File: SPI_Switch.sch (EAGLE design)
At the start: 43 parts, among them Q1 MOSFET-NCHANNELBSS123LT1G, Q2 MOSFET-NCHANNELBSS123LT1G, Q3 MOSFET-NCHANNELBSS123LT1G, Q4 MOSFET-NCHANNELBSS123LT1G, Q5 MOSFET-NCHANNELBSS123LT1G, Q6 MOSFET-NCHANNELBSS123LT1G, Q7 MOSFET-NCHANNELBSS123LT1G

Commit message: adding daniel's changes
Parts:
- removed Q1, Q2, Q3, Q4, Q5, Q6, Q7: MOSFET-NCHANNELBSS123LT1G, SparkFun-DiscreteSemi:MOSFET-NCHANNELBSS123LT1G
- R5: value DNP -> 1k
- renumbered U$1 to J3, U$2 to J1, U$3 to J5, U$4 to U2, U$5 to U1, U$6 to J2, U$7 to J4
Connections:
- removed net N$10: LED5.C, Q5.D
- removed net N$12: LED6.C, Q6.D
- removed net N$14: LED7.C, Q7.D
- removed net N$2: LED1.C, Q1.D
- removed net N$4: LED2.C, Q2.D
- removed net N$6: LED3.C, Q3.D
- removed net N$8: LED4.C, Q4.D
- net +24V: now also R5.1
- net CH1: now also LED1.C; no longer J1.4_PATH1, Q1.G
- net CH2: now also LED2.C; no longer J1.6_PATH2, Q2.G
- net CH3: now also LED3.C; no longer J1.8_PATH3, Q3.G
- net CH4: now also LED4.C; no longer J1.10_PATH4, Q4.G
- net CH5: now also LED5.C; no longer J1.12_PATH5, Q5.G
- net CH6: now also LED6.C; no longer J1.14_PATH6, Q6.G
- net CH7: now also LED7.C; no longer Q7.G
- net CH8: now also R5.2; no longer R5.1
- net GND: now also U1.2_IN; no longer Q1.S, Q2.S, Q3.S, Q4.S, Q5.S, Q6.S, Q7.S, R5.2
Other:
- moved on the sheet: LED1, LED2, LED3, LED4, LED5, LED6, LED7, R10, R11, R12, R5, R6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

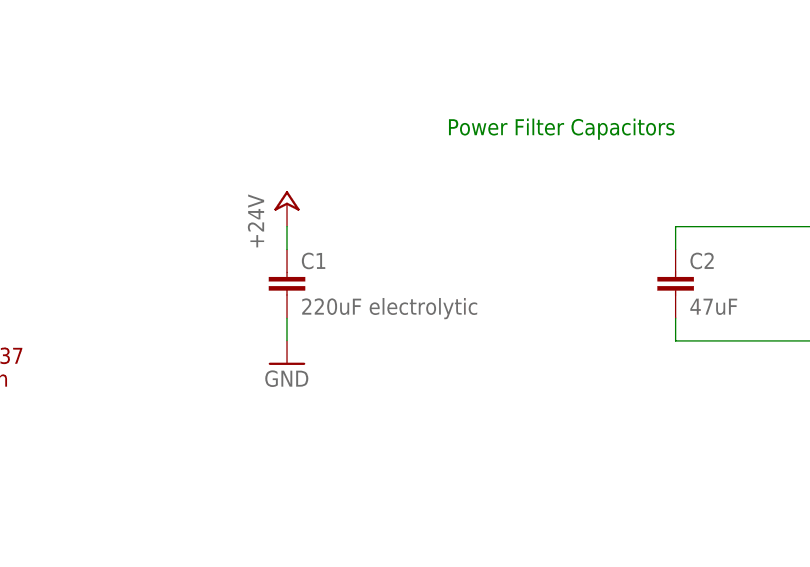
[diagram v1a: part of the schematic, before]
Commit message: Adding part numbers
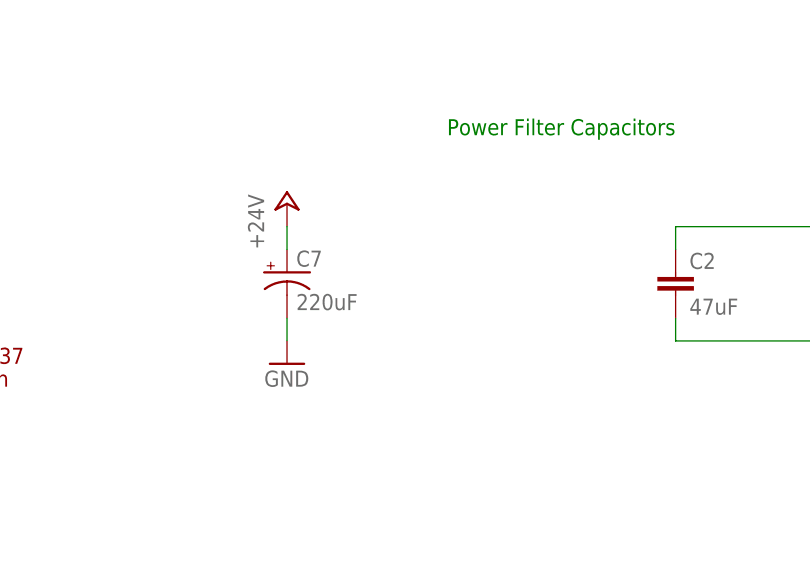
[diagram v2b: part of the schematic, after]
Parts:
- removed C1: 220uF electrolytic, SparkFun-Passives:CAP0805
- added C7: 220uF, SparkFun-Passives:CAP_POLE
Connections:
- net +24V: now also C7.+; no longer C1.1
- net GND: now also C7.-; no longer C1.2
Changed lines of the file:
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@@
 <part name="J2" library="SPI_Switch" deviceset="1-406525-1" device=""/>
 <part name="J4" library="SPI_Switch" deviceset="0705510037" device=""/>
-<part name="C1" library="SparkFun-Passives" deviceset="CAP" device="0805" value="220uF electrolytic"/>
 <part name="C2" library="SparkFun-Passives" deviceset="CAP" device="0805" value="47uF"/>
 <part name="C3" library="SparkFun-Passives" deviceset="CAP" device="0805" value="10uF"/>
@@
 <part name="P+17" library="supply1" deviceset="+24V" device=""/>
 <part name="J1" library="SPI_Switch" deviceset="8516-4500PL" device=""/>
+<part name="C7" library="SparkFun-Passives" deviceset="CAP_POL" device="E" value="220uF"/>
 </parts>
 <sheets>
@@
 <instance part="J2" gate="G$1" x="347.98" y="142.24"/>
 <instance part="J4" gate="G$1" x="104.14" y="40.64"/>
-<instance part="C1" gate="G$1" x="147.32" y="45.72"/>
 <instance part="C2" gate="G$1" x="190.5" y="45.72"/>
 <instance part="C3" gate="G$1" x="210.82" y="45.72"/>
@@
 <instance part="P+17" gate="1" x="299.72" y="335.28"/>
 <instance part="J1" gate="G$1" x="355.6" y="266.7"/>
+<instance part="C7" gate="G$1" x="147.32" y="48.26"/>
 </instances>
 <busses>
@@
 </segment>
 <segment>
-<pinref part="C1" gate="G$1" pin="2"/>
 <pinref part="GND2" gate="1" pin="GND"/>
 <wire x1="147.32" y1="43.18" x2="147.32" y2="40.64" width="0.1524" layer="91"/>
+<pinref part="C7" gate="G$1" pin="-"/>
 </segment>
 <segment>
@@
 <segment>
 <pinref part="P+3" gate="1" pin="+24V"/>
-<pinref part="C1" gate="G$1" pin="1"/>
 <wire x1="147.32" y1="53.34" x2="147.32" y2="50.8" width="0.1524" layer="91"/>
-</segment>
-<segment>
+<pinref part="C7" gate="G$1" pin="+"/>
+</segment>
+<segment>

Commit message: finished BOM
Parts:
- added LED8, LED9: YELLOW, SparkFun-LED:LED1206
- added R13: 2k, SparkFun-Passives:RESISTOR2512
- added R14: 330, SparkFun-Passives:RESISTOR0805-RES
- LED1, LED2, LED3, LED4, LED5, LED6, LED7: device led:LED -> SparkFun-LED:LED1206
- R10, R11, R12, R5, R6, R7, R8, R9: value 1k -> 2k; device SparkFun-Passives:RESISTOR0805-RES -> SparkFun-Passives:RESISTOR2512
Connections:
- new net N$2: LED8.A, R5.1
- new net N$4: LED9.A, R14.1
- net +24V: now also R10.2, R11.2, R12.2, R13.2, R5.2, R6.2, R7.2, R8.2, R9.2; no longer R10.1, R11.1, R12.1, R5.1, R6.1, R7.1, R8.1, R9.1
- net +5V: now also R14.2
- net CH8: now also R13.1; no longer R5.2
- net GND: now also LED8.C, LED9.C
- net N$1: now also R6.1; no longer R7.2
- net N$11: now also R11.1; no longer R11.2
- net N$13: now also R12.1; no longer R12.2
- net N$3: now also R7.1; no longer R6.2
- net N$5: now also R8.1; no longer R8.2
- net N$7: now also R9.1; no longer R9.2
- net N$9: now also R10.1; no longer R10.2
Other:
- note added: "Power Indication LEDs"
- moved on the sheet: R10, R11, R12, R5, R6, R7, R8, R9

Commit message: Finished layout, must do routing now
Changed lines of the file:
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@@
 <pinref part="U1" gate="G$1" pin="21_OUT0"/>
 <wire x1="180.34" y1="297.18" x2="208.28" y2="297.18" width="0.1524" layer="91"/>
-<wire x1="208.28" y1="297.18" x2="342.9" y2="297.18" width="0.1524" layer="91"/>
 <label x="187.96" y="297.18" size="1.778" layer="95"/>
 <label x="325.12" y="297.18" size="1.778" layer="95"/>
-<wire x1="208.28" y1="309.88" x2="208.28" y2="297.18" width="0.1524" layer="91"/>
-<junction x="208.28" y="297.18"/>
+<wire x1="208.28" y1="297.18" x2="342.9" y2="297.18" width="0.1524" layer="91"/>
 <wire x1="342.9" y1="297.18" x2="342.9" y2="302.26" width="0.1524" layer="91"/>
 <wire x1="342.9" y1="302.26" x2="350.52" y2="302.26" width="0.1524" layer="91"/>
 <pinref part="J1" gate="G$1" pin="3_PATH1"/>
 <pinref part="LED1" gate="G$1" pin="C"/>
-</segment>
-</net>
-<net name="N$1" class="0">
-<segment>
-<wire x1="208.28" y1="317.5" x2="208.28" y2="320.04" width="0.1524" layer="91"/>
-<pinref part="LED1" gate="G$1" pin="A"/>
-<pinref part="R6" gate="G$1" pin="1"/>
+<wire x1="208.28" y1="309.88" x2="208.28" y2="297.18" width="0.1524" layer="91"/>
+<junction x="208.28" y="297.18"/>
 </segment>
 </net>
@@
 <label x="187.96" y="294.64" size="1.778" layer="95"/>
 <label x="325.12" y="294.64" size="1.778" layer="95"/>
+<pinref part="J1" gate="G$1" pin="5_PATH2"/>
+<pinref part="LED2" gate="G$1" pin="C"/>
 <wire x1="220.98" y1="309.88" x2="220.98" y2="294.64" width="0.1524" layer="91"/>
 <junction x="220.98" y="294.64"/>
-<pinref part="J1" gate="G$1" pin="5_PATH2"/>
-<pinref part="LED2" gate="G$1" pin="C"/>
 </segment>
 </net>
@@
 <pinref part="U1" gate="G$1" pin="3_OUT2"/>
 <wire x1="180.34" y1="292.1" x2="233.68" y2="292.1" width="0.1524" layer="91"/>
-<wire x1="233.68" y1="292.1" x2="350.52" y2="292.1" width="0.1524" layer="91"/>
 <label x="187.96" y="292.1" size="1.778" layer="95"/>
 <label x="325.12" y="292.1" size="1.778" layer="95"/>
+<pinref part="J1" gate="G$1" pin="7_PATH3"/>
+<pinref part="LED3" gate="G$1" pin="C"/>
+<wire x1="233.68" y1="292.1" x2="350.52" y2="292.1" width="0.1524" layer="91"/>
 <wire x1="233.68" y1="309.88" x2="233.68" y2="292.1" width="0.1524" layer="91"/>
 <junction x="233.68" y="292.1"/>
-<pinref part="J1" gate="G$1" pin="7_PATH3"/>
-<pinref part="LED3" gate="G$1" pin="C"/>
 </segment>
 </net>
@@
 <pinref part="U1" gate="G$1" pin="4_OUT3"/>
 <wire x1="180.34" y1="289.56" x2="246.38" y2="289.56" width="0.1524" layer="91"/>
-<wire x1="246.38" y1="289.56" x2="345.44" y2="289.56" width="0.1524" layer="91"/>
 <label x="187.96" y="289.56" size="1.778" layer="95"/>
 <label x="325.12" y="289.56" size="1.778" layer="95"/>
-<wire x1="246.38" y1="309.88" x2="246.38" y2="289.56" width="0.1524" layer="91"/>
-<junction x="246.38" y="289.56"/>
+<wire x1="246.38" y1="289.56" x2="345.44" y2="289.56" width="0.1524" layer="91"/>
 <wire x1="345.44" y1="289.56" x2="345.44" y2="287.02" width="0.1524" layer="91"/>
 <wire x1="345.44" y1="287.02" x2="350.52" y2="287.02" width="0.1524" layer="91"/>
 <pinref part="J1" gate="G$1" pin="9_PATH4"/>
 <pinref part="LED4" gate="G$1" pin="C"/>
+<wire x1="246.38" y1="309.88" x2="246.38" y2="289.56" width="0.1524" layer="91"/>
+<junction x="246.38" y="289.56"/>
 </segment>
 </net>
@@
 <pinref part="U1" gate="G$1" pin="9_OUT4"/>
 <wire x1="180.34" y1="287.02" x2="259.08" y2="287.02" width="0.1524" layer="91"/>
-<wire x1="259.08" y1="287.02" x2="342.9" y2="287.02" width="0.1524" layer="91"/>
 <label x="187.96" y="287.02" size="1.778" layer="95"/>
 <label x="325.12" y="287.02" size="1.778" layer="95"/>
-<wire x1="259.08" y1="309.88" x2="259.08" y2="287.02" width="0.1524" layer="91"/>
-<junction x="259.08" y="287.02"/>
+<wire x1="259.08" y1="287.02" x2="342.9" y2="287.02" width="0.1524" layer="91"/>
 <wire x1="342.9" y1="287.02" x2="342.9" y2="281.94" width="0.1524" layer="91"/>
 <wire x1="342.9" y1="281.94" x2="350.52" y2="281.94" width="0.1524" layer="91"/>
 <pinref part="J1" gate="G$1" pin="11_PATH5"/>
 <pinref part="LED5" gate="G$1" pin="C"/>
+<wire x1="259.08" y1="309.88" x2="259.08" y2="287.02" width="0.1524" layer="91"/>
+<junction x="259.08" y="287.02"/>
 </segment>
 </net>
@@
 <pinref part="U1" gate="G$1" pin="10_OUT5"/>
 <wire x1="180.34" y1="284.48" x2="271.78" y2="284.48" width="0.1524" layer="91"/>
-<wire x1="271.78" y1="284.48" x2="340.36" y2="284.48" width="0.1524" layer="91"/>
 <label x="187.96" y="284.48" size="1.778" layer="95"/>
 <label x="325.12" y="284.48" size="1.778" layer="95"/>
-<wire x1="271.78" y1="309.88" x2="271.78" y2="284.48" width="0.1524" layer="91"/>
-<junction x="271.78" y="284.48"/>
+<wire x1="271.78" y1="284.48" x2="340.36" y2="284.48" width="0.1524" layer="91"/>
 <wire x1="340.36" y1="284.48" x2="340.36" y2="276.86" width="0.1524" layer="91"/>
 <wire x1="340.36" y1="276.86" x2="350.52" y2="276.86" width="0.1524" layer="91"/>
 <pinref part="J1" gate="G$1" pin="13_PATH6"/>
 <pinref part="LED6" gate="G$1" pin="C"/>
+<wire x1="271.78" y1="309.88" x2="271.78" y2="284.48" width="0.1524" layer="91"/>
+<junction x="271.78" y="284.48"/>
 </segment>
 </net>
@@
 <label x="187.96" y="281.94" size="1.778" layer="95"/>
 <label x="325.12" y="281.94" size="1.778" layer="95"/>
+<pinref part="J1" gate="G$1" pin="16_OPENALL"/>
+<pinref part="LED7" gate="G$1" pin="C"/>
 <wire x1="284.48" y1="309.88" x2="284.48" y2="281.94" width="0.1524" layer="91"/>
 <junction x="284.48" y="281.94"/>
-<pinref part="J1" gate="G$1" pin="16_OPENALL"/>
-<pinref part="LED7" gate="G$1" pin="C"/>
-</segment>
-</net>
-<net name="N$3" class="0">
-<segment>
-<wire x1="220.98" y1="317.5" x2="220.98" y2="320.04" width="0.1524" layer="91"/>
-<pinref part="LED2" gate="G$1" pin="A"/>
-<pinref part="R7" gate="G$1" pin="1"/>
-</segment>
-</net>
-<net name="N$5" class="0">
-<segment>
-<wire x1="233.68" y1="317.5" x2="233.68" y2="320.04" width="0.1524" layer="91"/>
-<pinref part="LED3" gate="G$1" pin="A"/>
-<pinref part="R8" gate="G$1" pin="1"/>
-</segment>
-</net>
-<net name="N$7" class="0">
-<segment>
-<wire x1="246.38" y1="317.5" x2="246.38" y2="320.04" width="0.1524" layer="91"/>
-<pinref part="LED4" gate="G$1" pin="A"/>
-<pinref part="R9" gate="G$1" pin="1"/>
-</segment>
-</net>
-<net name="N$9" class="0">
-<segment>
-<wire x1="259.08" y1="317.5" x2="259.08" y2="320.04" width="0.1524" layer="91"/>
-<pinref part="LED5" gate="G$1" pin="A"/>
-<pinref part="R10" gate="G$1" pin="1"/>
-</segment>
-</net>
-<net name="N$11" class="0">
-<segment>
-<wire x1="271.78" y1="317.5" x2="271.78" y2="320.04" width="0.1524" layer="91"/>
-<pinref part="LED6" gate="G$1" pin="A"/>
-<pinref part="R11" gate="G$1" pin="1"/>
-</segment>
-</net>
-<net name="N$13" class="0">
-<segment>
-<wire x1="284.48" y1="317.5" x2="284.48" y2="320.04" width="0.1524" layer="91"/>
-<pinref part="LED7" gate="G$1" pin="A"/>
-<pinref part="R12" gate="G$1" pin="1"/>
 </segment>
 </net>
@@
 </segment>
 </net>
+<net name="N$1" class="0">
+<segment>
+<pinref part="LED1" gate="G$1" pin="A"/>
+<pinref part="R6" gate="G$1" pin="1"/>
+<wire x1="208.28" y1="317.5" x2="208.28" y2="320.04" width="0.1524" layer="91"/>
+</segment>
+</net>
+<net name="N$3" class="0">
+<segment>
+<pinref part="R7" gate="G$1" pin="1"/>
+<pinref part="LED2" gate="G$1" pin="A"/>
+<wire x1="220.98" y1="320.04" x2="220.98" y2="317.5" width="0.1524" layer="91"/>
+</segment>
+</net>
+<net name="N$5" class="0">
+<segment>
+<pinref part="R8" gate="G$1" pin="1"/>
+<pinref part="LED3" gate="G$1" pin="A"/>
+<wire x1="233.68" y1="320.04" x2="233.68" y2="317.5" width="0.1524" layer="91"/>
+</segment>
+</net>
+<net name="N$6" class="0">
+<segment>
+<pinref part="R9" gate="G$1" pin="1"/>
+<pinref part="LED4" gate="G$1" pin="A"/>
+<wire x1="246.38" y1="320.04" x2="246.38" y2="317.5" width="0.1524" layer="91"/>
+</segment>
+</net>
+<net name="N$7" class="0">
+<segment>
+<pinref part="R10" gate="G$1" pin="1"/>
+<pinref part="LED5" gate="G$1" pin="A"/>
+<wire x1="259.08" y1="320.04" x2="259.08" y2="317.5" width="0.1524" layer="91"/>
+</segment>
+</net>
+<net name="N$8" class="0">
+<segment>
+<pinref part="R11" gate="G$1" pin="1"/>
+<pinref part="LED6" gate="G$1" pin="A"/>
+<wire x1="271.78" y1="320.04" x2="271.78" y2="317.5" width="0.1524" layer="91"/>
+</segment>
+</net>
+<net name="N$9" class="0">
+<segment>
+<pinref part="R12" gate="G$1" pin="1"/>
+<pinref part="LED7" gate="G$1" pin="A"/>
+<wire x1="284.48" y1="320.04" x2="284.48" y2="317.5" width="0.1524" layer="91"/>
+</segment>
+</net>

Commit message: Added channel routings
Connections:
- net CE: now also U1.1_CS
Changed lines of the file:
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@@
 <pinref part="R4" gate="G$1" pin="1"/>
 <wire x1="185.42" y1="101.6" x2="233.68" y2="101.6" width="0.1524" layer="91"/>
+<pinref part="U1" gate="G$1" pin="1_CS"/>
 </segment>
 </net>

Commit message: Finished routing except ground plane
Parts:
- removed C6: 10uF, SparkFun-Passives:CAP0805
- added C1: (no value), SparkFun-Passives:CAP0402-CAP
- C5: value 10uF -> (none); device SparkFun-Passives:CAP0805 -> SparkFun-Passives:CAP0402-CAP
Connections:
- net +5V: now also C1.1; no longer C6.1
- net GND: now also C1.2; no longer C6.2
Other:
- moved on the sheet: C5
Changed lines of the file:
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@@
 <part name="P+6" library="supply1" deviceset="+5V" device=""/>
 <part name="GND7" library="supply1" deviceset="GND" device=""/>
-<part name="C5" library="SparkFun-Passives" deviceset="CAP" device="0805" value="10uF"/>
-<part name="C6" library="SparkFun-Passives" deviceset="CAP" device="0805" value="10uF"/>
 <part name="P+7" library="supply1" deviceset="+5V" device=""/>
 <part name="P+8" library="supply1" deviceset="+5V" device=""/>
@@
 <part name="R13" library="SparkFun-Passives" deviceset="RESISTOR" device="2512" value="2k"/>
 <part name="R14" library="SparkFun-Passives" deviceset="RESISTOR" device="0805-RES" value="330"/>
+<part name="C1" library="SparkFun-Passives" deviceset="CAP" device="0402-CAP"/>
+<part name="C5" library="SparkFun-Passives" deviceset="CAP" device="0402-CAP"/>
 </parts>
 <sheets>
@@
 <instance part="P+6" gate="1" x="231.14" y="182.88"/>
 <instance part="GND7" gate="1" x="340.36" y="137.16"/>
-<instance part="C5" gate="G$1" x="81.28" y="302.26"/>
-<instance part="C6" gate="G$1" x="96.52" y="302.26"/>
 <instance part="P+7" gate="1" x="81.28" y="312.42"/>
 <instance part="P+8" gate="1" x="96.52" y="312.42"/>
@@
 <instance part="R13" gate="G$1" x="299.72" y="325.12" rot="R90"/>
 <instance part="R14" gate="G$1" x="96.52" y="363.22" rot="R90"/>
+<instance part="C1" gate="G$1" x="81.28" y="302.26"/>
+<instance part="C5" gate="G$1" x="96.52" y="302.26"/>
 </instances>
 <busses>
@@
 </segment>
 <segment>
-<pinref part="C5" gate="G$1" pin="2"/>
 <wire x1="81.28" y1="299.72" x2="81.28" y2="297.18" width="0.1524" layer="91"/>
 <pinref part="GND8" gate="1" pin="GND"/>
-</segment>
-<segment>
-<pinref part="C6" gate="G$1" pin="2"/>
+<pinref part="C1" gate="G$1" pin="2"/>
+</segment>
+<segment>
 <wire x1="96.52" y1="299.72" x2="96.52" y2="297.18" width="0.1524" layer="91"/>
 <pinref part="GND9" gate="1" pin="GND"/>
+<pinref part="C5" gate="G$1" pin="2"/>
 </segment>
 <segment>
@@
 </segment>
 <segment>
-<pinref part="C5" gate="G$1" pin="1"/>
 <wire x1="81.28" y1="307.34" x2="81.28" y2="309.88" width="0.1524" layer="91"/>
 <pinref part="P+7" gate="1" pin="+5V"/>
-</segment>
-<segment>
-<pinref part="C6" gate="G$1" pin="1"/>
+<pinref part="C1" gate="G$1" pin="1"/>
+</segment>
+<segment>
 <wire x1="96.52" y1="307.34" x2="96.52" y2="309.88" width="0.1524" layer="91"/>
 <pinref part="P+8" gate="1" pin="+5V"/>
-</segment>
-<segment>
+<pinref part="C5" gate="G$1" pin="1"/>
+</segment>
+<segment>

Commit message: Replaced decoupling caps for line driver with a larger package. Added smaller resistors for LEDs. Must ensure we never pull over 20mA with this resistor package.
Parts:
- C1, C5: value (none) -> 10uF; device SparkFun-Passives:CAP0402-CAP -> SparkFun-Passives:CAP0805
- R10, R11, R12, R13, R6, R7, R8, R9: value 2k -> 1.5k; device SparkFun-Passives:RESISTOR2512 -> SparkFun-Passives:RESISTOR1206
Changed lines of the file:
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@@
 <part name="P+19" library="supply1" deviceset="+5V" device=""/>
 <part name="R5" library="SparkFun-Passives" deviceset="RESISTOR" device="2512" value="2k"/>
-<part name="R6" library="SparkFun-Passives" deviceset="RESISTOR" device="2512" value="2k"/>
-<part name="R7" library="SparkFun-Passives" deviceset="RESISTOR" device="2512" value="2k"/>
-<part name="R8" library="SparkFun-Passives" deviceset="RESISTOR" device="2512" value="2k"/>
-<part name="R9" library="SparkFun-Passives" deviceset="RESISTOR" device="2512" value="2k"/>
-<part name="R10" library="SparkFun-Passives" deviceset="RESISTOR" device="2512" value="2k"/>
-<part name="R11" library="SparkFun-Passives" deviceset="RESISTOR" device="2512" value="2k"/>
-<part name="R12" library="SparkFun-Passives" deviceset="RESISTOR" device="2512" value="2k"/>
-<part name="R13" library="SparkFun-Passives" deviceset="RESISTOR" device="2512" value="2k"/>
 <part name="R14" library="SparkFun-Passives" deviceset="RESISTOR" device="0805-RES" value="330"/>
-<part name="C1" library="SparkFun-Passives" deviceset="CAP" device="0402-CAP"/>
-<part name="C5" library="SparkFun-Passives" deviceset="CAP" device="0402-CAP"/>
+<part name="C1" library="SparkFun-Passives" deviceset="CAP" device="0805" value="10uF"/>
+<part name="C5" library="SparkFun-Passives" deviceset="CAP" device="0805" value="10uF"/>
+<part name="R6" library="SparkFun-Passives" deviceset="RESISTOR" device="1206" value="1.5k"/>
+<part name="R7" library="SparkFun-Passives" deviceset="RESISTOR" device="1206" value="1.5k"/>
+<part name="R8" library="SparkFun-Passives" deviceset="RESISTOR" device="1206" value="1.5k"/>
+<part name="R9" library="SparkFun-Passives" deviceset="RESISTOR" device="1206" value="1.5k"/>
+<part name="R10" library="SparkFun-Passives" deviceset="RESISTOR" device="1206" value="1.5k"/>
+<part name="R11" library="SparkFun-Passives" deviceset="RESISTOR" device="1206" value="1.5k"/>
+<part name="R12" library="SparkFun-Passives" deviceset="RESISTOR" device="1206" value="1.5k"/>
+<part name="R13" library="SparkFun-Passives" deviceset="RESISTOR" device="1206" value="1.5k"/>
 </parts>
 <sheets>
@@
 <instance part="P+19" gate="1" x="96.52" y="373.38"/>
 <instance part="R5" gate="G$1" x="81.28" y="363.22" rot="R90"/>
+<instance part="R14" gate="G$1" x="96.52" y="363.22" rot="R90"/>
+<instance part="C1" gate="G$1" x="81.28" y="302.26"/>
+<instance part="C5" gate="G$1" x="96.52" y="302.26"/>
 <instance part="R6" gate="G$1" x="208.28" y="325.12" rot="R90"/>
 <instance part="R7" gate="G$1" x="220.98" y="325.12" rot="R90"/>
@@
 <instance part="R12" gate="G$1" x="284.48" y="325.12" rot="R90"/>
 <instance part="R13" gate="G$1" x="299.72" y="325.12" rot="R90"/>
-<instance part="R14" gate="G$1" x="96.52" y="363.22" rot="R90"/>
-<instance part="C1" gate="G$1" x="81.28" y="302.26"/>
-<instance part="C5" gate="G$1" x="96.52" y="302.26"/>
 </instances>
 <busses>
@@
 <segment>
 <pinref part="LED1" gate="G$1" pin="A"/>
+<wire x1="208.28" y1="317.5" x2="208.28" y2="320.04" width="0.1524" layer="91"/>
 <pinref part="R6" gate="G$1" pin="1"/>
-<wire x1="208.28" y1="317.5" x2="208.28" y2="320.04" width="0.1524" layer="91"/>
 </segment>
 </net>
 <net name="N$3" class="0">
 <segment>
-<pinref part="R7" gate="G$1" pin="1"/>
 <pinref part="LED2" gate="G$1" pin="A"/>
 <wire x1="220.98" y1="320.04" x2="220.98" y2="317.5" width="0.1524" layer="91"/>
+<pinref part="R7" gate="G$1" pin="1"/>
 </segment>
 </net>
 <net name="N$5" class="0">
 <segment>
-<pinref part="R8" gate="G$1" pin="1"/>
 <pinref part="LED3" gate="G$1" pin="A"/>
 <wire x1="233.68" y1="320.04" x2="233.68" y2="317.5" width="0.1524" layer="91"/>
+<pinref part="R8" gate="G$1" pin="1"/>
 </segment>
 </net>
 <net name="N$6" class="0">
 <segment>
-<pinref part="R9" gate="G$1" pin="1"/>
 <pinref part="LED4" gate="G$1" pin="A"/>
 <wire x1="246.38" y1="320.04" x2="246.38" y2="317.5" width="0.1524" layer="91"/>
+<pinref part="R9" gate="G$1" pin="1"/>
 </segment>
 </net>
 <net name="N$7" class="0">
 <segment>
-<pinref part="R10" gate="G$1" pin="1"/>
 <pinref part="LED5" gate="G$1" pin="A"/>
 <wire x1="259.08" y1="320.04" x2="259.08" y2="317.5" width="0.1524" layer="91"/>
+<pinref part="R10" gate="G$1" pin="1"/>
 </segment>
 </net>
 <net name="N$8" class="0">
 <segment>
-<pinref part="R11" gate="G$1" pin="1"/>
 <pinref part="LED6" gate="G$1" pin="A"/>
 <wire x1="271.78" y1="320.04" x2="271.78" y2="317.5" width="0.1524" layer="91"/>
+<pinref part="R11" gate="G$1" pin="1"/>
 </segment>
 </net>
 <net name="N$9" class="0">
 <segment>
-<pinref part="R12" gate="G$1" pin="1"/>
 <pinref part="LED7" gate="G$1" pin="A"/>
 <wire x1="284.48" y1="320.04" x2="284.48" y2="317.5" width="0.1524" layer="91"/>
-</segment>
-</net>
+<pinref part="R12" gate="G$1" pin="1"/>
+</segment>
+</net>
